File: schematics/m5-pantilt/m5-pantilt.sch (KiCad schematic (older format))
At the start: 28 parts, among them J1 Conn_02x15_Odd_Even, J2 Conn_02x03_Odd_Even, J3 Conn_02x03_Odd_Even, J4 Conn_01x04, J5 BAT, J6 Conn_01x04, J7 5V_POWER, SW1 SW_SPDT, U1 TC7WH241FK

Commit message: Refine schematics
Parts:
- added Q1: IRLML6402, Package_TO_SOT_SMD:SOT-23, symbol Transistor_FET:IRLML6402
- added R5: 1k, symbol Device:R
- SW1: footprint Button_Switch_THT:SW_E-Switch_EG1224_SPDT_Angled -> Button_Switch_THT:SW_CuK_OS102011MA1QN1_SPDT_Angled; URL (none) -> https://www.digikey.jp/ja/products/detail/c-k/OS102011MA1QN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
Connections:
- net GND: now also SW1.1 (A)
- net at D1.2 (A), J1.29 (Pin_29): now also Q1.2 (S); no longer SW1.3 (C)
- net at J5.1 (Pin_1): now also Q1.3 (D), R5.2; no longer SW1.2 (B)
- new net: Q1.1 (G), R5.1, SW1.2 (B)
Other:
- moved on the sheet: J5, SW1
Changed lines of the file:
@@
 L power:PWR_FLAG #FLG0101
 U 1 1 60C7066B
-P 2700 5100
-F 0 "#FLG0101" H 2700 5175 50  0001 C CNN
-F 1 "PWR_FLAG" H 2700 5273 50  0000 C CNN
-F 2 "" H 2700 5100 50  0001 C CNN
-F 3 "~" H 2700 5100 50  0001 C CNN
-	1    2700 5100
+P 1150 5250
+F 0 "#FLG0101" H 1150 5325 50  0001 C CNN
+F 1 "PWR_FLAG" H 1150 5423 50  0000 C CNN
+F 2 "" H 1150 5250 50  0001 C CNN
+F 3 "~" H 1150 5250 50  0001 C CNN
+	1    1150 5250
 	1    0    0    -1
 $EndComp
@@
 L Connector_Generic:Conn_01x02 J5
 U 1 1 60C74B9F
-P 2000 5350
-F 0 "J5" H 1918 5567 50  0000 C CNN
-F 1 "BAT" H 1918 5476 50  0000 C CNN
-F 2 "Connector_JST:JST_PH_B2B-PH-K_1x02_P2.00mm_Vertical" H 2000 5350 50  0001 C CNN
-F 3 "~" H 2000 5350 50  0001 C CNN
-F 4 "https://akizukidenshi.com/catalog/g/gC-12802/" H 2000 5350 50  0001 C CNN "URL"
-	1    2000 5350
+P 800 5450
+F 0 "J5" H 718 5667 50  0000 C CNN
+F 1 "BAT" H 718 5576 50  0000 C CNN
+F 2 "Connector_JST:JST_PH_B2B-PH-K_1x02_P2.00mm_Vertical" H 800 5450 50  0001 C CNN
+F 3 "~" H 800 5450 50  0001 C CNN
+F 4 "https://akizukidenshi.com/catalog/g/gC-12802/" H 800 5450 50  0001 C CNN "URL"
+	1    800  5450
 	-1   0    0    -1
 $EndComp
@@
 L power:GND #PWR0102
 U 1 1 60C7D8E0
-P 2300 5650
-F 0 "#PWR0102" H 2300 5400 50  0001 C CNN
-F 1 "GND" H 2305 5477 50  0000 C CNN
-F 2 "" H 2300 5650 50  0001 C CNN
-F 3 "" H 2300 5650 50  0001 C CNN
-	1    2300 5650
+P 1450 6600
+F 0 "#PWR0102" H 1450 6350 50  0001 C CNN
+F 1 "GND" H 1455 6427 50  0000 C CNN
+F 2 "" H 1450 6600 50  0001 C CNN
+F 3 "" H 1450 6600 50  0001 C CNN
+	1    1450 6600
 	1    0    0    -1
 $EndComp
@@
 L Switch:SW_SPDT SW1
 U 1 1 60CC23E9
-P 2400 5350
-F 0 "SW1" H 2400 5635 50  0000 C CNN
-F 1 "SW_SPDT" H 2400 5544 50  0000 C CNN
-F 2 "Button_Switch_THT:SW_E-Switch_EG1224_SPDT_Angled" H 2400 5350 50  0001 C CNN
-F 3 "~" H 2400 5350 50  0001 C CNN
-	1    2400 5350
-	1    0    0    -1
-$EndComp
-Wire Wire Line
-	2200 5450 2300 5450
-Wire Wire Line
-	2300 5450 2300 5650
+P 1350 6150
+F 0 "SW1" V 1450 6450 50  0000 C CNN
+F 1 "SW_SPDT" V 1350 6400 50  0000 C CNN
+F 2 "Button_Switch_THT:SW_CuK_OS102011MA1QN1_SPDT_Angled" H 1350 6150 50  0001 C CNN
+F 3 "~" H 1350 6150 50  0001 C CNN
+F 4 "https://www.digikey.jp/ja/products/detail/c-k/OS102011MA1QN1/1981430" H 1350 6150 50  0001 C CNN "URL"
+	1    1350 6150
+	0    1    1    0
+$EndComp
+Wire Wire Line
+	1450 6350 1450 6500
 $Comp
 L power:PWR_FLAG #FLG0105
@@
 Wire Wire Line
 	2050 3800 2050 3950
-NoConn ~ 2600 5250
-Wire Wire Line
-	2700 5450 2600 5450
 Text Label 4150 4750 0    50   ~ 0
 PWM2_C1
@@
 	3350 5150 3550 5150
 Wire Wire Line
-	2700 5100 2700 5450
-Wire Wire Line
 	3550 5250 3550 5450
 Wire Wire Line
 	3550 5450 3350 5450
-Wire Wire Line
-	3350 5450 2700 5450
 Connection ~ 3350 5450
-Connection ~ 2700 5450
 $Comp
 L Jumper:Jumper_2_Open JP2
@@
 Wire Wire Line
 	3100 5150 3350 5150
-$Comp
-L power:+5V #PWR012
-U 1 1 6113153F
-P 2300 6200
-F 0 "#PWR012" H 2300 6050 50  0001 C CNN
-F 1 "+5V" H 2400 6200 50  0000 C CNN
-F 2 "" H 2300 6200 50  0001 C CNN
-F 3 "" H 2300 6200 50  0001 C CNN
-	1    2300 6200
-	1    0    0    -1
-$EndComp
 Wire Wire Line
 	2300 6200 2300 6300
@@
 	-1   0    0    1
 $EndComp
+$Comp
+L Device:R R5
+U 1 1 61DEC6ED
+P 1350 5650
+F 0 "R5" H 1280 5604 50  0000 R CNN
+F 1 "1k" H 1280 5695 50  0000 R CNN
+F 2 "" V 1280 5650 50  0001 C CNN
+F 3 "~" H 1350 5650 50  0001 C CNN
+	1    1350 5650
+	-1   0    0    1
+$EndComp
+Wire Wire Line
+	1150 5450 1000 5450
+Wire Wire Line
+	1150 5250 1150 5450
+Connection ~ 1150 5450
+Wire Wire Line
+	1150 5450 1350 5450
+Wire Wire Line
+	1350 5450 1350 5500
+Wire Wire Line
+	1950 5450 3350 5450
+NoConn ~ 1250 6350
+Wire Wire Line
+	1350 5800 1350 5900
+$Comp
+L Transistor_FET:IRLML6402 Q1
+U 1 1 61DDC391
+P 1750 5550
+F 0 "Q1" V 2092 5550 50  0000 C CNN
+F 1 "IRLML6402" V 2001 5550 50  0000 C CNN
+F 2 "Package_TO_SOT_SMD:SOT-23" H 1950 5475 50  0001 L CIN
+F 3 "https://www.infineon.com/dgdl/irlml6402pbf.pdf?fileId=5546d462533600a401535668d5c2263c" H 1750 5550 50  0001 L CNN
+F 4 "https://akizukidenshi.com/catalog/g/gI-02553/" H 1750 5550 50  0001 C CNN "URL"
+	1    1750 5550
+	0    -1   -1   0
+$EndComp
+Wire Wire Line
+	1350 5450 1550 5450
+Connection ~ 1350 5450
+Wire Wire Line
+	1750 5750 1750 5900
+Wire Wire Line
+	1750 5900 1350 5900
+Connection ~ 1350 5900
+Wire Wire Line
+	1350 5900 1350 5950
+$Comp
+L power:+5V #PWR012
+U 1 1 61F185A4
+P 2300 6200
+F 0 "#PWR012" H 2300 6050 50  0001 C CNN
+F 1 "+5V" H 2400 6200 50  0000 C CNN
+F 2 "" H 2300 6200 50  0001 C CNN
+F 3 "" H 2300 6200 50  0001 C CNN
+	1    2300 6200
+	1    0    0    -1
+$EndComp
+Wire Wire Line
+	1000 5550 1000 6500
+Wire Wire Line
+	1000 6500 1450 6500
+Connection ~ 1450 6500
+Wire Wire Line
+	1450 6500 1450 6600
 $EndSCHEMATC

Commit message: generate gerber files
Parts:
- R5: footprint (none) -> Resistor_SMD:R_0603_1608Metric_Pad1.05x0.95mm_HandSolder
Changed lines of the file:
@@
 F 0 "R5" H 1280 5604 50  0000 R CNN
 F 1 "1k" H 1280 5695 50  0000 R CNN
-F 2 "" V 1280 5650 50  0001 C CNN
+F 2 "Resistor_SMD:R_0603_1608Metric_Pad1.05x0.95mm_HandSolder" V 1280 5650 50  0001 C CNN
 F 3 "~" H 1350 5650 50  0001 C CNN
 	1    1350 5650

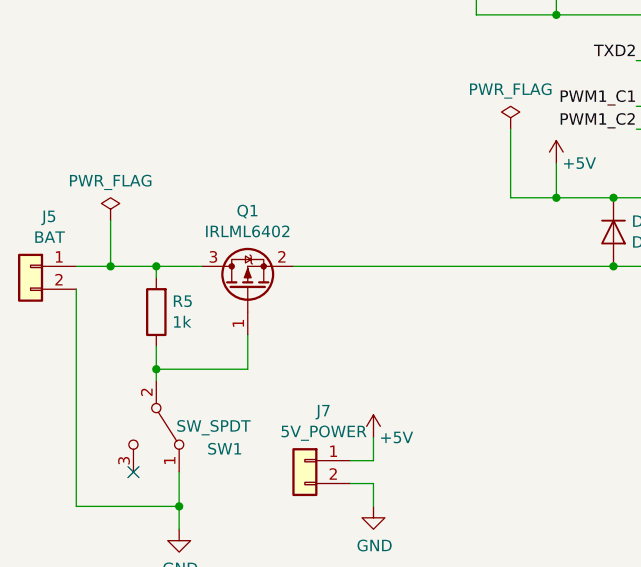
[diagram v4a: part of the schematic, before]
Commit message: Fix MOSFET direction
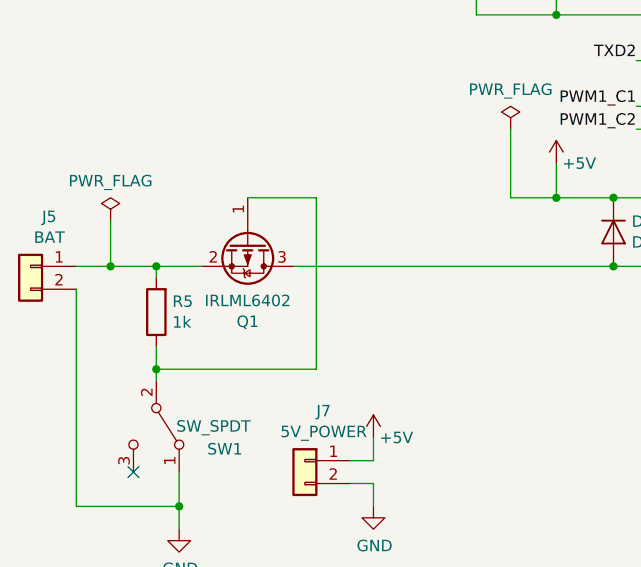
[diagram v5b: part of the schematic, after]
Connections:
- net at D1.2 (A), J1.29 (Pin_29): now also Q1.3 (D); no longer Q1.2 (S)
- net at J5.1 (Pin_1), R5.2: now also Q1.2 (S); no longer Q1.3 (D)
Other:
- moved on the sheet: Q1
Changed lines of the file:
@@
 L Transistor_FET:IRLML6402 Q1
 U 1 1 61DDC391
-P 1750 5550
-F 0 "Q1" V 2092 5550 50  0000 C CNN
-F 1 "IRLML6402" V 2001 5550 50  0000 C CNN
-F 2 "Package_TO_SOT_SMD:SOT-23" H 1950 5475 50  0001 L CIN
-F 3 "https://www.infineon.com/dgdl/irlml6402pbf.pdf?fileId=5546d462533600a401535668d5c2263c" H 1750 5550 50  0001 L CNN
-F 4 "https://akizukidenshi.com/catalog/g/gI-02553/" H 1750 5550 50  0001 C CNN "URL"
-	1    1750 5550
-	0    -1   -1   0
+P 1750 5350
+F 0 "Q1" V 2092 5350 50  0000 C CNN
+F 1 "IRLML6402" V 2001 5350 50  0000 C CNN
+F 2 "Package_TO_SOT_SMD:SOT-23" H 1950 5275 50  0001 L CIN
+F 3 "https://www.infineon.com/dgdl/irlml6402pbf.pdf?fileId=5546d462533600a401535668d5c2263c" H 1750 5350 50  0001 L CNN
+F 4 "https://akizukidenshi.com/catalog/g/gI-02553/" H 1750 5350 50  0001 C CNN "URL"
+	1    1750 5350
+	0    1    1    0
 $EndComp
 Wire Wire Line
 	1350 5450 1550 5450
 Connection ~ 1350 5450
-Wire Wire Line
-	1750 5750 1750 5900
-Wire Wire Line
-	1750 5900 1350 5900
 Connection ~ 1350 5900
 Wire Wire Line
@@
 Wire Wire Line
 	1450 6500 1450 6600
+Wire Wire Line
+	2050 5150 1750 5150
+Wire Wire Line
+	1350 5900 2050 5900
+Wire Wire Line
+	2050 5150 2050 5900
 $EndSCHEMATC

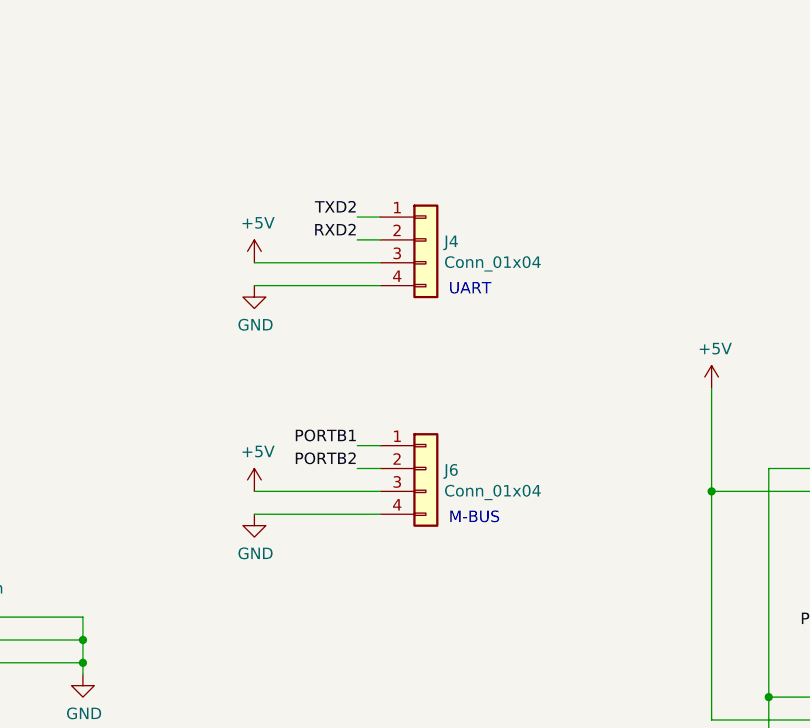
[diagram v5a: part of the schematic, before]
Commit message: Fix #61 port bc assign (#62)
* Fix pin assign

* Fix silk

* Regenerate gerber
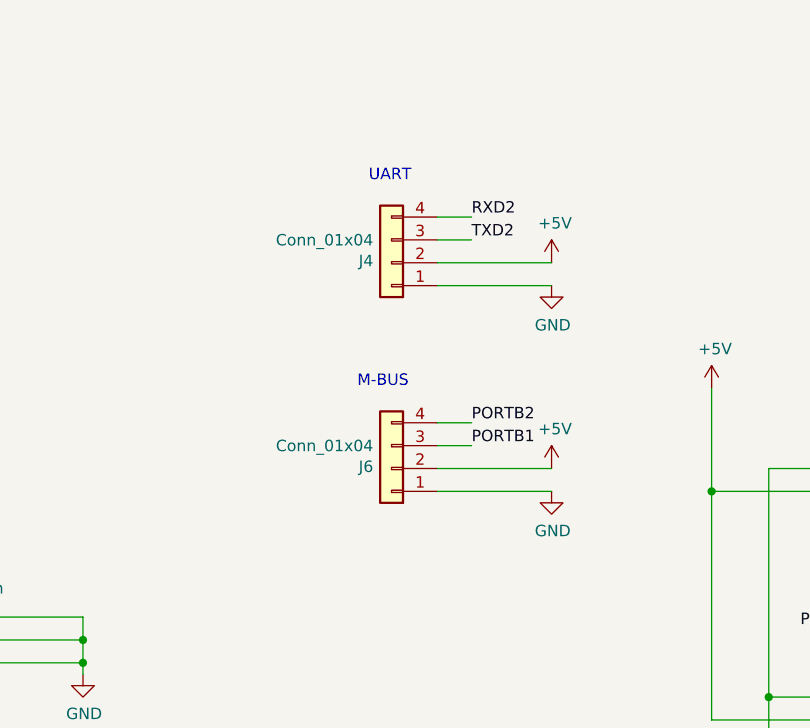
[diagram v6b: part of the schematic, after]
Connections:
- net +5V: now also J4.2 (Pin_2), J6.2 (Pin_2); no longer J4.3 (Pin_3), J6.3 (Pin_3)
- net GND: now also J4.1 (Pin_1), J6.1 (Pin_1); no longer J4.4 (Pin_4), J6.4 (Pin_4)
- net PORTB1: now also J6.3 (Pin_3); no longer J6.1 (Pin_1)
- net PORTB2: now also J6.4 (Pin_4); no longer J6.2 (Pin_2)
- net RXD2: now also J4.4 (Pin_4); no longer J4.2 (Pin_2)
- net TXD2: now also J4.3 (Pin_3); no longer J4.1 (Pin_1)
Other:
- moved on the sheet: J6
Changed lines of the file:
@@
 L Connector_Generic:Conn_01x04 J6
 U 1 1 60C9A55E
-P 6050 3200
-F 0 "J6" H 6130 3192 50  0000 L CNN
-F 1 "Conn_01x04" H 6130 3101 50  0000 L CNN
-F 2 "Connector_JST:JST_PH_S4B-PH-K_1x04_P2.00mm_Horizontal" H 6050 3200 50  0001 C CNN
-F 3 "~" H 6050 3200 50  0001 C CNN
-	1    6050 3200
-	1    0    0    -1
-$EndComp
-Text Label 5750 3100 2    50   ~ 0
+P 5900 3200
+F 0 "J6" H 5980 3192 50  0000 L CNN
+F 1 "Conn_01x04" H 5980 3101 50  0000 L CNN
+F 2 "Connector_JST:JST_PH_S4B-PH-K_1x04_P2.00mm_Horizontal" H 5900 3200 50  0001 C CNN
+F 3 "~" H 5900 3200 50  0001 C CNN
+	1    5900 3200
+	-1   0    0    1
+$EndComp
+Text Label 6250 3100 0    50   ~ 0
 PORTB1
-Wire Wire Line
-	5750 3100 5850 3100
-Text Label 5750 3200 2    50   ~ 0
+Text Label 6250 3000 0    50   ~ 0
 PORTB2
-Wire Wire Line
-	5750 3200 5850 3200
 $Comp
 L power:+5V #PWR09
 U 1 1 60C9EE6D
-P 5300 3300
-F 0 "#PWR09" H 5300 3150 50  0001 C CNN
-F 1 "+5V" H 5315 3473 50  0000 C CNN
-F 2 "" H 5300 3300 50  0001 C CNN
-F 3 "" H 5300 3300 50  0001 C CNN
-	1    5300 3300
-	1    0    0    -1
-$EndComp
-Wire Wire Line
-	5300 3300 5850 3300
+P 6600 3200
+F 0 "#PWR09" H 6600 3050 50  0001 C CNN
+F 1 "+5V" H 6615 3373 50  0000 C CNN
+F 2 "" H 6600 3200 50  0001 C CNN
+F 3 "" H 6600 3200 50  0001 C CNN
+	1    6600 3200
+	1    0    0    -1
+$EndComp
 $Comp
 L power:GND #PWR010
 U 1 1 60CA11B5
-P 5300 3400
-F 0 "#PWR010" H 5300 3150 50  0001 C CNN
-F 1 "GND" H 5305 3227 50  0000 C CNN
-F 2 "" H 5300 3400 50  0001 C CNN
-F 3 "" H 5300 3400 50  0001 C CNN
-	1    5300 3400
-	1    0    0    -1
-$EndComp
-Wire Wire Line
-	5300 3400 5850 3400
+P 6600 3300
+F 0 "#PWR010" H 6600 3050 50  0001 C CNN
+F 1 "GND" H 6605 3127 50  0000 C CNN
+F 2 "" H 6600 3300 50  0001 C CNN
+F 3 "" H 6600 3300 50  0001 C CNN
+	1    6600 3300
+	1    0    0    -1
+$EndComp
 $Comp
 L Switch:SW_SPDT SW1
@@
 L Connector_Generic:Conn_01x04 J4
 U 1 1 60CA66E1
-P 6050 2200
-F 0 "J4" H 6130 2192 50  0000 L CNN
-F 1 "Conn_01x04" H 6130 2101 50  0000 L CNN
-F 2 "Connector_JST:JST_PH_S4B-PH-K_1x04_P2.00mm_Horizontal" H 6050 2200 50  0001 C CNN
-F 3 "~" H 6050 2200 50  0001 C CNN
-F 4 "https://www.sengoku.co.jp/mod/sgk_cart/detail.php?code=EEHD-55FC" H 6050 2200 50  0001 C CNN "URL"
-	1    6050 2200
-	1    0    0    -1
-$EndComp
-Wire Wire Line
-	5750 2100 5850 2100
-Wire Wire Line
-	5750 2200 5850 2200
+P 5900 2300
+F 0 "J4" H 5980 2292 50  0000 L CNN
+F 1 "Conn_01x04" H 5980 2201 50  0000 L CNN
+F 2 "Connector_JST:JST_PH_S4B-PH-K_1x04_P2.00mm_Horizontal" H 5900 2300 50  0001 C CNN
+F 3 "~" H 5900 2300 50  0001 C CNN
+F 4 "https://www.sengoku.co.jp/mod/sgk_cart/detail.php?code=EEHD-55FC" H 5900 2300 50  0001 C CNN "URL"
+	1    5900 2300
+	-1   0    0    1
+$EndComp
 $Comp
 L power:+5V #PWR01
 U 1 1 60CA66EB
-P 5300 2300
-F 0 "#PWR01" H 5300 2150 50  0001 C CNN
-F 1 "+5V" H 5315 2473 50  0000 C CNN
-F 2 "" H 5300 2300 50  0001 C CNN
-F 3 "" H 5300 2300 50  0001 C CNN
-	1    5300 2300
-	1    0    0    -1
-$EndComp
-Wire Wire Line
-	5300 2300 5850 2300
+P 6600 2300
+F 0 "#PWR01" H 6600 2150 50  0001 C CNN
+F 1 "+5V" H 6615 2473 50  0000 C CNN
+F 2 "" H 6600 2300 50  0001 C CNN
+F 3 "" H 6600 2300 50  0001 C CNN
+	1    6600 2300
+	1    0    0    -1
+$EndComp
 $Comp
 L power:GND #PWR011
 U 1 1 60CA66F2
-P 5300 2400
-F 0 "#PWR011" H 5300 2150 50  0001 C CNN
-F 1 "GND" H 5305 2227 50  0000 C CNN
-F 2 "" H 5300 2400 50  0001 C CNN
-F 3 "" H 5300 2400 50  0001 C CNN
-	1    5300 2400
-	1    0    0    -1
-$EndComp
-Wire Wire Line
-	5300 2400 5850 2400
-Text Label 5750 2100 2    50   ~ 0
+P 6600 2400
+F 0 "#PWR011" H 6600 2150 50  0001 C CNN
+F 1 "GND" H 6605 2227 50  0000 C CNN
+F 2 "" H 6600 2400 50  0001 C CNN
+F 3 "" H 6600 2400 50  0001 C CNN
+	1    6600 2400
+	1    0    0    -1
+$EndComp
+Text Label 6250 2200 0    50   ~ 0
 TXD2
-Text Label 5750 2200 2    50   ~ 0
+Text Label 6250 2100 0    50   ~ 0
 RXD2
 Wire Wire Line
@@
 Text Notes 8250 5400 0    50   ~ 0
 Short JP1, JP2 for PWM Servo\nShort JP3, JP4 for Serial Servo
-Text Notes 6150 3450 0    50   ~ 0
+Text Notes 5750 2850 0    50   ~ 0
 M-BUS
-Text Notes 6150 2450 0    50   ~ 0
+Text Notes 5800 1950 0    50   ~ 0
 UART
 Wire Wire Line
@@
 Wire Wire Line
 	2050 5150 2050 5900
+Wire Wire Line
+	6100 2100 6250 2100
+Wire Wire Line
+	6100 2200 6250 2200
+Wire Wire Line
+	6100 2300 6600 2300
+Wire Wire Line
+	6100 2400 6600 2400
+Wire Wire Line
+	6100 3000 6250 3000
+Wire Wire Line
+	6100 3100 6250 3100
+Wire Wire Line
+	6100 3200 6600 3200
+Wire Wire Line
+	6100 3300 6600 3300
 $EndSCHEMATC

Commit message: Fix/schematics review (#69)
* WIP: fix schematics

* WIP: fix schematics

* fix schematics

* fix schematics

* fix schematics

* Fix board assembly instruction

* Plot gerber
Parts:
- removed D1: D, Diode_SMD:D_SMA_Handsoldering, symbol Device:D
- removed JP1, JP10, JP2, JP3, JP4, JP5, JP6, JP7, JP8, JP9: Jumper_2_Open, Jumper:SolderJumper-2_P1.3mm_Open_Pad1.0x1.5mm, symbol Jumper:Jumper_2_Open
- added R10, R11, R12, R13, R14, R15, R16, R9: 0, Resistor_SMD:R_0603_1608Metric_Pad1.05x0.95mm_HandSolder, symbol Device:R
- added R6: 10k, Resistor_SMD:R_0603_1608Metric_Pad1.05x0.95mm_HandSolder, symbol Device:R
- R5: value 1k -> 47k
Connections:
- net +3V3: now also R16.1, R6.2
- net GND: now also R15.2
- net PWM1: now also R10.1, R9.1
- net PWM1_C1: now also R9.2
- net PWM1_C2: now also R10.2
- net PWM2: now also R11.1, R12.1
- net PWM2_C1: now also R11.2
- net PWM2_C2: now also R12.2
- net TXD2: now also R6.1
- net at U1.7 (2OE): now also R15.1, R16.2
- net at J3.2 (Pin_2), J3.5 (Pin_5): now also R4.1, R13.1, R14.2
- net at R2.1: now also R14.1
- net at J2.2 (Pin_2), J2.5 (Pin_5): now also R3.1, R13.2
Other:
- note added: "Short R10, R10 for Core2\nShort R9, R11 for others"
- note added: "Short R13, R14 for Serial Servo"
- note removed: "Short JP1, JP2 for PWM Servo\nShort JP3, JP4 for Serial Servo"
- note removed: "Short JP6, JP8 for Core2\nShort JP5, JP7 for others"

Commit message: WIP: new board
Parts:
- removed J2, J3: Conn_02x03_Odd_Even, Connector_PinHeader_2.54mm:PinHeader_2x03_P2.54mm_Vertical, symbol Connector_Generic:Conn_02x03_Odd_Even
- removed R1: 1k, Resistor_SMD:R_0603_1608Metric_Pad1.05x0.95mm_HandSolder, symbol Device:R
- removed R15, R16: 0, Resistor_SMD:R_0603_1608Metric_Pad1.05x0.95mm_HandSolder, symbol Device:R
- removed R2: 100, Resistor_SMD:R_0603_1608Metric_Pad1.05x0.95mm_HandSolder, symbol Device:R
- removed R6: 10k, Resistor_SMD:R_0603_1608Metric_Pad1.05x0.95mm_HandSolder, symbol Device:R
- removed U1: TC7WH241FK, m5-pantilt:NL27WZ125USG, symbol pantilt:TC7WH241FK
- added 2.2k (x2), 20k: R, symbol Device:R
- added C?: 0.1u, symbol Device:C
- added D?: D, symbol Device:D
- added J?: Conn_02x15_Odd_Even, symbol Connector_Generic:Conn_02x15_Odd_Even
- added J? (x2): Conn_01x03, symbol Connector_Generic:Conn_01x03
- added Q?: 2SA1015, Package_TO_SOT_THT:TO-92_Inline, symbol Transistor_BJT:2SA1015
- added U?: MAX3485, symbol Interface_UART:MAX3485
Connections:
- net +3V3: now also 2.2k.1, C?.1, J?.11 (Pin_11), Q?.2 (C), U?.8 (VCC)
- net +5V: now also D?.1 (K), J?.2 (Pin_2), J?.2 (Pin_2), J?.27 (Pin_27); no longer J7.1 (Pin_1)
- net GND: now also 2.2k.2, 20k.2, C?.2, J?.1 (Pin_1), J?.1 (Pin_1), J?.2 (Pin_2), J?.4 (Pin_4), J?.6 (Pin_6), U?.5 (GND)
- net PORTB1: now also J?.9 (Pin_9)
- net PORTB2: now also J?.3 (Pin_3)
- net PWM1_C1: now also J?.19 (Pin_19)
- net PWM1_C2: now also J?.21 (Pin_21)
- net PWM2_C1: now also J?.20 (Pin_20)
- net PWM2_C2: now also J?.22 (Pin_22)
- net RXD2: now also J?.16 (Pin_16), U?.1 (RO)
- net TXD2: now also J?.15 (Pin_15), Q?.3 (B), U?.4 (DI)
- net PIN1: now reaches J1.1 (Pin_1)
- net PIN1: now also J?.1 (Pin_1)
- net PIN10: now reaches J1.10 (Pin_10)
- net PIN10: now also J?.10 (Pin_10)
- net PIN12: now reaches J1.12 (Pin_12)
- net PIN12: now also J?.12 (Pin_12)
- net PIN13: now reaches J1.13 (Pin_13)
- net PIN13: now also J?.13 (Pin_13)
- net PIN14: now reaches J1.14 (Pin_14)
- net PIN14: now also J?.14 (Pin_14)
- net PIN17: now reaches J1.17 (Pin_17)
- net PIN17: now also J?.17 (Pin_17)
- net PIN18: now reaches J1.18 (Pin_18)
- net PIN18: now also J?.18 (Pin_18)
- net PIN23: now reaches J1.23 (Pin_23)
- net PIN23: now also J?.23 (Pin_23)
- net PIN24: now reaches J1.24 (Pin_24)
- net PIN24: now also J?.24 (Pin_24)
- net PIN25: now reaches J1.25 (Pin_25)
- net PIN25: now also J?.25 (Pin_25)
- net PIN26: now reaches J1.26 (Pin_26)
- net PIN26: now also J?.26 (Pin_26)
- net PIN28: now reaches J1.28 (Pin_28)
- net PIN28: now also J?.28 (Pin_28)
- net BAT: now reaches J1.29 (Pin_29), Q1.3 (D)
- net BAT: now also J?.29 (Pin_29)
- net PIN30: now reaches J1.30 (Pin_30)
- net PIN30: now also J?.30 (Pin_30)
- net PIN5: now reaches J1.5 (Pin_5)
- net PIN5: now also J?.5 (Pin_5)
- net PIN7: now reaches J1.7 (Pin_7)
- net PIN7: now also J?.7 (Pin_7)
- net PIN8: now reaches J1.8 (Pin_8)
- net PIN8: now also J?.8 (Pin_8)
- net at R13.1, R14.2, R4.1: now also J?.3 (Pin_3)
- net TTL: now reaches R14.1
- net TTL: now also U?.6 (A)
- net at R13.2, R3.1: now also J?.3 (Pin_3)
- new net: D?.2 (A), J7.1 (Pin_1)
- new net: 20k.1, Q?.1 (E), U?.2 (~RE), U?.3 (DE)
- new net: 2.2k.1, 2.2k.2, U?.7 (B)
- no-connect marks 21 -> 1
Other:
- note removed: "Short JP10 to pull-up if 2OE is not inverted,\nShort JP9 to pull-down if 2OE is inverted like 1OE.\n(Depends on IC)"
- moved on the sheet: J1, J7
